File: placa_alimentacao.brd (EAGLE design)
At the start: 55.5 x 39.4 mm, 8 parts, among them IC1 7803TV

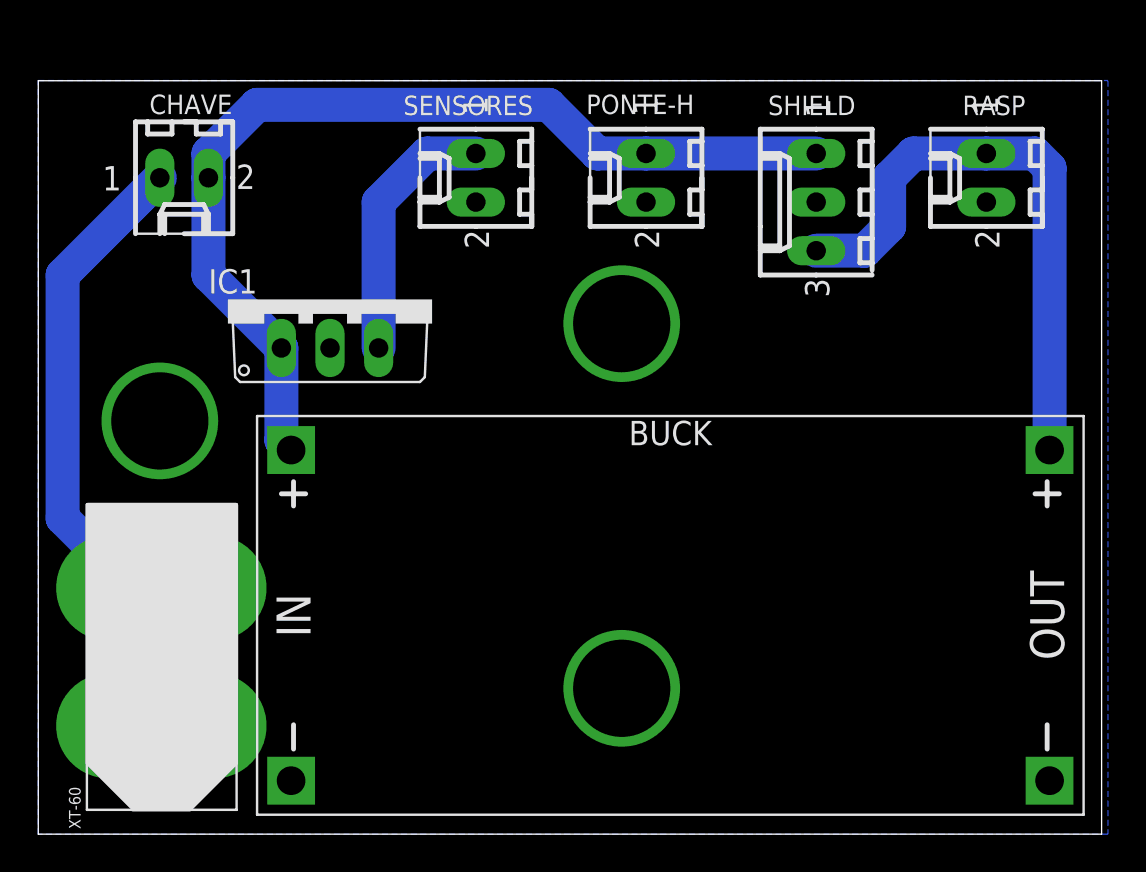
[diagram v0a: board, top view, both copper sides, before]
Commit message: Modificação do tamanho da placa
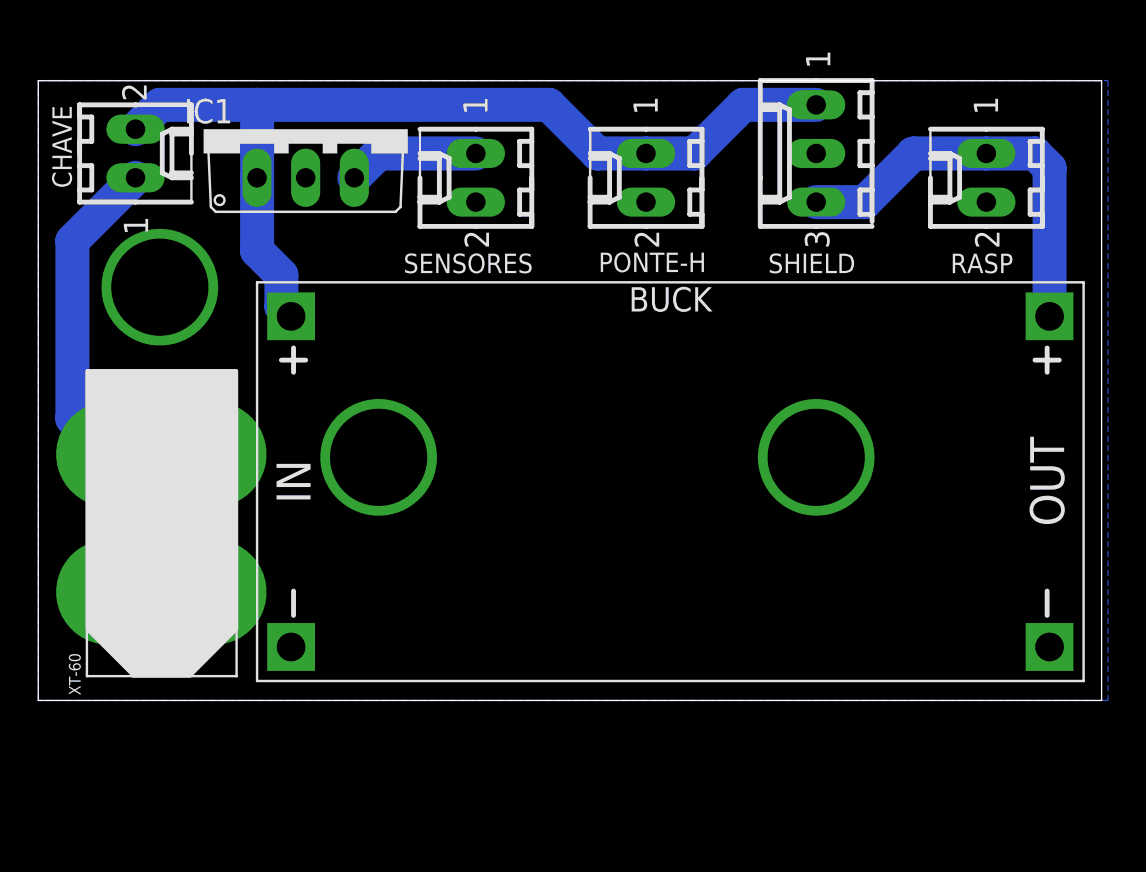
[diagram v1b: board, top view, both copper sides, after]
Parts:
- moved IC1 8.98 mm to (11.4, 40.6)
- moved BUCK 6.99 mm to (30.5, 22.2)
- moved XT-60 6.98 mm to (2.54, 17.1)
- moved CHAVE 2.84 mm to (2.54, 39.4), turned to 270 degrees
- moved SHIELD 2.54 mm to (38.1, 39.4)
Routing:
- net +5V: track 30.8 -> 21.3 mm
- net N$1: track 26.6 -> 19.4 mm
- net +5V/1: track 13.8 -> 6.88 mm
- net +8V: track 51.1 -> 50.0 mm
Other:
- board size 55.5 x 39.4 mm -> 55.5 x 32.4 mm
